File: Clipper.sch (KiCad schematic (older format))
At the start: 38 parts

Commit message: Added component numbers.
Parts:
- gave numbers to parts that had none: 35
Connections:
- net AGND: now also U17.3 (+), U17.5 (+), U18.3 (+); no longer U17.3 (+), U17.5 (+), U18.5 (+)
- net LOUT: now also U17.1; no longer U17.7
- net at R37.2, R38.2, R39.2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: now also U17.2 (_); no longer U17.6 (_)
- net at D20.1 (A), R41.2, R43.1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: now also U17.6 (_); no longer U17.2 (_)
- net at D20.2 (K), D22.1 (A): now also U17.7; no longer U17.1
- net at D21.1 (A), R42.2, R44.2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: now also U18.2 (_); no longer U18.6 (_)
- net at D21.2 (K), D23.1 (A): now also U18.1; no longer U18.7
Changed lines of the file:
@@
 LOUT
 $Comp
-L R R?
+L R R31
 U 1 1 536E7249
 P 1450 3050
-F 0 "R?" V 1530 3050 40  0000 C CNN
+F 0 "R31" V 1530 3050 40  0000 C CNN
 F 1 "12k" V 1450 3050 40  0000 C CNN
 F 2 "~" V 1380 3050 30  0000 C CNN
@@
 $EndComp
 $Comp
-L R R?
+L R R33
 U 1 1 536E7262
 P 1850 2600
-F 0 "R?" V 1930 2600 40  0000 C CNN
+F 0 "R33" V 1930 2600 40  0000 C CNN
 F 1 "30k" V 1857 2601 40  0000 C CNN
 F 2 "~" V 1780 2600 30  0000 C CNN
@@
 $EndComp
 $Comp
-L LM4562 U?
+L LM4562 U16
 U 1 1 536E7276
 P 2500 3150
-F 0 "U?" H 2750 3000 60  0000 L CNN
+F 0 "U16" H 2750 3000 60  0000 L CNN
 F 1 "LM4562" H 2750 2900 60  0000 L CNN
 F 2 "~" H 2600 3150 60  0000 C CNN
@@
 -15V
 $Comp
-L DIODE D?
+L DIODE D16
 U 1 1 536E72A5
 P 2600 2550
-F 0 "D?" H 2600 2650 40  0000 C CNN
+F 0 "D16" H 2600 2650 40  0000 C CNN
 F 1 "1N4148" H 2600 2450 40  0000 C CNN
 F 2 "~" H 2600 2550 60  0000 C CNN
@@
 $EndComp
 $Comp
-L DIODE D?
+L DIODE D18
 U 1 1 536E72BC
 P 2900 2250
-F 0 "D?" H 2900 2350 40  0000 C CNN
+F 0 "D18" H 2900 2350 40  0000 C CNN
 F 1 "1N4148" H 2900 2150 40  0000 C CNN
 F 2 "~" H 2900 2250 60  0000 C CNN
@@
 $EndComp
 $Comp
-L R R?
+L R R35
 U 1 1 536E72D9
 P 2350 2250
-F 0 "R?" V 2430 2250 40  0000 C CNN
+F 0 "R35" V 2430 2250 40  0000 C CNN
 F 1 "12k" V 2357 2251 40  0000 C CNN
 F 2 "~" V 2280 2250 30  0000 C CNN
@@
 +15V
 $Comp
-L R R?
+L R R32
 U 1 1 536E799F
 P 1450 4950
-F 0 "R?" V 1530 4950 40  0000 C CNN
+F 0 "R32" V 1530 4950 40  0000 C CNN
 F 1 "12k" V 1450 4950 40  0000 C CNN
 F 2 "~" V 1380 4950 30  0000 C CNN
@@
 $EndComp
 $Comp
-L R R?
+L R R34
 U 1 1 536E79A5
 P 1850 5400
-F 0 "R?" V 1930 5400 40  0000 C CNN
+F 0 "R34" V 1930 5400 40  0000 C CNN
 F 1 "30k" V 1857 5401 40  0000 C CNN
 F 2 "~" V 1780 5400 30  0000 C CNN
@@
 $EndComp
 $Comp
-L LM4562 U?
+L LM4562 U16
 U 2 1 536E79AB
 P 2500 5050
-F 0 "U?" H 2750 4900 60  0000 L CNN
+F 0 "U16" H 2750 4900 60  0000 L CNN
 F 1 "LM4562" H 2750 4800 60  0000 L CNN
 F 2 "~" H 2600 5050 60  0000 C CNN
@@
 -15V
 $Comp
-L DIODE D?
+L DIODE D17
 U 1 1 536E79B4
 P 2600 4450
-F 0 "D?" H 2600 4550 40  0000 C CNN
+F 0 "D17" H 2600 4550 40  0000 C CNN
 F 1 "1N4148" H 2600 4350 40  0000 C CNN
 F 2 "~" H 2600 4450 60  0000 C CNN
@@
 $EndComp
 $Comp
-L DIODE D?
+L DIODE D19
 U 1 1 536E79BA
 P 2900 4150
-F 0 "D?" H 2900 4250 40  0000 C CNN
+F 0 "D19" H 2900 4250 40  0000 C CNN
 F 1 "1N4148" H 2900 4050 40  0000 C CNN
 F 2 "~" H 2900 4150 60  0000 C CNN
@@
 $EndComp
 $Comp
-L R R?
+L R R36
 U 1 1 536E79C0
 P 2350 4150
-F 0 "R?" V 2430 4150 40  0000 C CNN
+F 0 "R36" V 2430 4150 40  0000 C CNN
 F 1 "12k" V 2357 4151 40  0000 C CNN
 F 2 "~" V 2280 4150 30  0000 C CNN
@@
 -15V
 $Comp
-L LM4562 U?
-U 2 1 536E7B83
+L LM4562 U17
+U 1 1 536E7B83
 P 4650 3800
-F 0 "U?" H 4900 3650 60  0000 L CNN
+F 0 "U17" H 4900 3650 60  0000 L CNN
 F 1 "LM4562" H 4900 3550 60  0000 L CNN
 F 2 "~" H 4750 3800 60  0000 C CNN
 F 3 "~" H 4750 3800 60  0000 C CNN
-	2    4650 3800
+	1    4650 3800
 	1    0    0    -1
 $EndComp
@@
 -15V
 $Comp
-L R R?
+L R R41
 U 1 1 536E8357
 P 6850 3050
-F 0 "R?" V 6930 3050 40  0000 C CNN
+F 0 "R41" V 6930 3050 40  0000 C CNN
 F 1 "12k" V 6850 3050 40  0000 C CNN
 F 2 "~" V 6780 3050 30  0000 C CNN
@@
 $EndComp
 $Comp
-L R R?
+L R R43
 U 1 1 536E835D
 P 7250 2600
-F 0 "R?" V 7330 2600 40  0000 C CNN
+F 0 "R43" V 7330 2600 40  0000 C CNN
 F 1 "30k" V 7257 2601 40  0000 C CNN
 F 2 "~" V 7180 2600 30  0000 C CNN
@@
 $EndComp
 $Comp
-L LM4562 U?
-U 1 1 536E8363
+L LM4562 U17
+U 2 1 536E8363
 P 7900 3150
-F 0 "U?" H 8150 3000 60  0000 L CNN
+F 0 "U17" H 8150 3000 60  0000 L CNN
 F 1 "LM4562" H 8150 2900 60  0000 L CNN
 F 2 "~" H 8000 3150 60  0000 C CNN
 F 3 "~" H 8000 3150 60  0000 C CNN
-	1    7900 3150
+	2    7900 3150
 	1    0    0    -1
 $EndComp
@@
 -15V
 $Comp
-L DIODE D?
+L DIODE D20
 U 1 1 536E836C
 P 8000 2550
-F 0 "D?" H 8000 2650 40  0000 C CNN
+F 0 "D20" H 8000 2650 40  0000 C CNN
 F 1 "1N4148" H 8000 2450 40  0000 C CNN
 F 2 "~" H 8000 2550 60  0000 C CNN
@@
 $EndComp
 $Comp
-L DIODE D?
+L DIODE D22
 U 1 1 536E8372
 P 8300 2250
-F 0 "D?" H 8300 2350 40  0000 C CNN
+F 0 "D22" H 8300 2350 40  0000 C CNN
 F 1 "1N4148" H 8300 2150 40  0000 C CNN
 F 2 "~" H 8300 2250 60  0000 C CNN
@@
 $EndComp
 $Comp
-L R R?
+L R R45
 U 1 1 536E8378
 P 7750 2250
-F 0 "R?" V 7830 2250 40  0000 C CNN
+F 0 "R45" V 7830 2250 40  0000 C CNN
 F 1 "12k" V 7757 2251 40  0000 C CNN
 F 2 "~" V 7680 2250 30  0000 C CNN
@@
 +15V
 $Comp
-L R R?
+L R R42
 U 1 1 536E8391
 P 6850 4950
-F 0 "R?" V 6930 4950 40  0000 C CNN
+F 0 "R42" V 6930 4950 40  0000 C CNN
 F 1 "12k" V 6850 4950 40  0000 C CNN
 F 2 "~" V 6780 4950 30  0000 C CNN
@@
 $EndComp
 $Comp
-L R R?
+L R R44
 U 1 1 536E8397
 P 7250 5400
-F 0 "R?" V 7330 5400 40  0000 C CNN
+F 0 "R44" V 7330 5400 40  0000 C CNN
 F 1 "30k" V 7257 5401 40  0000 C CNN
 F 2 "~" V 7180 5400 30  0000 C CNN
@@
 $EndComp
 $Comp
-L LM4562 U?
-U 2 1 536E839D
+L LM4562 U18
+U 1 1 536E839D
 P 7900 5050
-F 0 "U?" H 8150 4900 60  0000 L CNN
+F 0 "U18" H 8150 4900 60  0000 L CNN
 F 1 "LM4562" H 8150 4800 60  0000 L CNN
 F 2 "~" H 8000 5050 60  0000 C CNN
 F 3 "~" H 8000 5050 60  0000 C CNN
-	2    7900 5050
+	1    7900 5050
 	1    0    0    -1
 $EndComp
@@
 -15V
 $Comp
-L DIODE D?
+L DIODE D21
 U 1 1 536E83A6
 P 8000 4450
-F 0 "D?" H 8000 4550 40  0000 C CNN
+F 0 "D21" H 8000 4550 40  0000 C CNN
 F 1 "1N4148" H 8000 4350 40  0000 C CNN
 F 2 "~" H 8000 4450 60  0000 C CNN
@@
 $EndComp
 $Comp
-L DIODE D?
+L DIODE D23
 U 1 1 536E83AC
 P 8300 4150
-F 0 "D?" H 8300 4250 40  0000 C CNN
+F 0 "D23" H 8300 4250 40  0000 C CNN
 F 1 "1N4148" H 8300 4050 40  0000 C CNN
 F 2 "~" H 8300 4150 60  0000 C CNN
@@
 $EndComp
 $Comp
-L R R?
+L R R46
 U 1 1 536E83B2
 P 7750 4150
-F 0 "R?" V 7830 4150 40  0000 C CNN
+F 0 "R46" V 7830 4150 40  0000 C CNN
 F 1 "12k" V 7757 4151 40  0000 C CNN
 F 2 "~" V 7680 4150 30  0000 C CNN
@@
 -15V
 $Comp
-L LM4562 U?
+L LM4562 U18
 U 2 1 536E83E9
 P 10050 3800
-F 0 "U?" H 10300 3650 60  0000 L CNN
+F 0 "U18" H 10300 3650 60  0000 L CNN
 F 1 "LM4562" H 10300 3550 60  0000 L CNN
 F 2 "~" H 10150 3800 60  0000 C CNN
@@
 Set to clip at +/- 6 V
 $Comp
-L C C?
+L C C38
 U 1 1 536EC1E0
 P 5450 1700
-F 0 "C?" H 5450 1800 40  0000 L CNN
+F 0 "C38" H 5450 1800 40  0000 L CNN
 F 1 "470n" H 5456 1615 40  0000 L CNN
 F 2 "~" H 5488 1550 30  0000 C CNN
@@
 	5250 1900 5800 1900
 $Comp
-L C C?
+L C C40
 U 1 1 537C3D88
 P 5800 1700
-F 0 "C?" H 5800 1800 40  0000 L CNN
+F 0 "C40" H 5800 1800 40  0000 L CNN
 F 1 "470n" H 5806 1615 40  0000 L CNN
 F 2 "~" H 5838 1550 30  0000 C CNN
@@
 $EndComp
 $Comp
-L C C?
+L C C39
 U 1 1 537C3D8F
 P 5450 2100
-F 0 "C?" H 5450 2200 40  0000 L CNN
+F 0 "C39" H 5450 2200 40  0000 L CNN
 F 1 "470n" H 5456 2015 40  0000 L CNN
 F 2 "~" H 5488 1950 30  0000 C CNN
@@
 $EndComp
 $Comp
-L C C?
+L C C41
 U 1 1 537C3D96
 P 5800 2100
-F 0 "C?" H 5800 2200 40  0000 L CNN
+F 0 "C41" H 5800 2200 40  0000 L CNN
 F 1 "470n" H 5806 2015 40  0000 L CNN
 F 2 "~" H 5838 1950 30  0000 C CNN
@@
 $EndComp
 $Comp
-L R R?
+L R R37
 U 1 1 537C500E
 P 3600 3400
-F 0 "R?" V 3680 3400 40  0000 C CNN
+F 0 "R37" V 3680 3400 40  0000 C CNN
 F 1 "2.2k" V 3607 3401 40  0000 C CNN
 F 2 "~" V 3530 3400 30  0000 C CNN
@@
 Noise calculation:\nFull scale approx. +/- 6V.\n24 bits, so LSB corresponds to approx. 12*2^(-24) = 0.72 uV.\nQucs analysis gives a pretty flat noise spectrum at around 0.4 uV, which passes.
 $Comp
-L R R?
+L R R38
 U 1 1 537CA2E9
 P 3600 3700
-F 0 "R?" V 3680 3700 40  0000 C CNN
+F 0 "R38" V 3680 3700 40  0000 C CNN
 F 1 "2.2k" V 3607 3701 40  0000 C CNN
 F 2 "~" V 3530 3700 30  0000 C CNN
@@
 $EndComp
 $Comp
-L R R?
+L R R39
 U 1 1 537CA2EF
 P 3600 4000
-F 0 "R?" V 3680 4000 40  0000 C CNN
+F 0 "R39" V 3680 4000 40  0000 C CNN
 F 1 "2.2k" V 3607 4001 40  0000 C CNN
 F 2 "~" V 3530 4000 30  0000 C CNN
@@
 $EndComp
 $Comp
-L R R?
+L R R40
 U 1 1 537CA2F5
 P 4750 3200
-F 0 "R?" V 4830 3200 40  0000 C CNN
+F 0 "R40" V 4830 3200 40  0000 C CNN
 F 1 "2.2k" V 4757 3201 40  0000 C CNN
 F 2 "~" V 4680 3200 30  0000 C CNN
@@
 $EndComp
 $Comp
-L R R?
+L R R47
 U 1 1 537CA2FB
 P 9000 3400
-F 0 "R?" V 9080 3400 40  0000 C CNN
+F 0 "R47" V 9080 3400 40  0000 C CNN
 F 1 "2.2k" V 9007 3401 40  0000 C CNN
 F 2 "~" V 8930 3400 30  0000 C CNN
@@
 $EndComp
 $Comp
-L R R?
+L R R48
 U 1 1 537CA301
 P 9000 3700
-F 0 "R?" V 9080 3700 40  0000 C CNN
+F 0 "R48" V 9080 3700 40  0000 C CNN
 F 1 "2.2k" V 9007 3701 40  0000 C CNN
 F 2 "~" V 8930 3700 30  0000 C CNN
@@
 $EndComp
 $Comp
-L R R?
+L R R49
 U 1 1 537CA307
 P 9000 4000
-F 0 "R?" V 9080 4000 40  0000 C CNN
+F 0 "R49" V 9080 4000 40  0000 C CNN
 F 1 "2.2k" V 9007 4001 40  0000 C CNN
 F 2 "~" V 8930 4000 30  0000 C CNN
@@
 $EndComp
 $Comp
-L R R?
+L R R50
 U 1 1 537CA30D
 P 10150 3200
-F 0 "R?" V 10230 3200 40  0000 C CNN
+F 0 "R50" V 10230 3200 40  0000 C CNN
 F 1 "2.2k" V 10157 3201 40  0000 C CNN
 F 2 "~" V 10080 3200 30  0000 C CNN

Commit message: Minor schematic mods, started assigning DigiKey part numbers to components.
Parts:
- C38, C39, C40, C41: DigiKey (none) -> 445-8425-ND; Type Ceramic -> (none)
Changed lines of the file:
@@
 LIBS:my-conn
 LIBS:ADC-cache
-EELAYER 27 0
+EELAYER 24 0
 EELAYER END
 $Descr A4 11693 8268
@@
 F 2 "~" H 5488 1550 30  0000 C CNN
 F 3 "~" H 5450 1700 60  0000 C CNN
-F 4 "Ceramic" H 5450 1700 60  0001 C CNN "Type"
+F 4 "445-8425-ND" H 5450 1700 60  0001 C CNN "DigiKey"
 	1    5450 1700
 	1    0    0    -1
@@
 Wire Wire Line
 	5250 1900 5800 1900
-$Comp
-L C C40
-U 1 1 537C3D88
-P 5800 1700
-F 0 "C40" H 5800 1800 40  0000 L CNN
-F 1 "470n" H 5806 1615 40  0000 L CNN
-F 2 "~" H 5838 1550 30  0000 C CNN
-F 3 "~" H 5800 1700 60  0000 C CNN
-F 4 "Ceramic" H 5800 1700 60  0001 C CNN "Type"
-	1    5800 1700
-	1    0    0    -1
-$EndComp
-$Comp
-L C C39
-U 1 1 537C3D8F
-P 5450 2100
-F 0 "C39" H 5450 2200 40  0000 L CNN
-F 1 "470n" H 5456 2015 40  0000 L CNN
-F 2 "~" H 5488 1950 30  0000 C CNN
-F 3 "~" H 5450 2100 60  0000 C CNN
-F 4 "Ceramic" H 5450 2100 60  0001 C CNN "Type"
-	1    5450 2100
-	1    0    0    -1
-$EndComp
-$Comp
-L C C41
-U 1 1 537C3D96
-P 5800 2100
-F 0 "C41" H 5800 2200 40  0000 L CNN
-F 1 "470n" H 5806 2015 40  0000 L CNN
-F 2 "~" H 5838 1950 30  0000 C CNN
-F 3 "~" H 5800 2100 60  0000 C CNN
-F 4 "Ceramic" H 5800 2100 60  0001 C CNN "Type"
-	1    5800 2100
-	1    0    0    -1
-$EndComp
 $Comp
 L R R37
@@
 	0    -1   -1   0
 $EndComp
+$Comp
+L C C40
+U 1 1 537D7769
+P 5800 1700
+F 0 "C40" H 5800 1800 40  0000 L CNN
+F 1 "470n" H 5806 1615 40  0000 L CNN
+F 2 "~" H 5838 1550 30  0000 C CNN
+F 3 "~" H 5800 1700 60  0000 C CNN
+F 4 "445-8425-ND" H 5800 1700 60  0001 C CNN "DigiKey"
+	1    5800 1700
+	1    0    0    -1
+$EndComp
+$Comp
+L C C39
+U 1 1 537D7778
+P 5450 2100
+F 0 "C39" H 5450 2200 40  0000 L CNN
+F 1 "470n" H 5456 2015 40  0000 L CNN
+F 2 "~" H 5488 1950 30  0000 C CNN
+F 3 "~" H 5450 2100 60  0000 C CNN
+F 4 "445-8425-ND" H 5450 2100 60  0001 C CNN "DigiKey"
+	1    5450 2100
+	1    0    0    -1
+$EndComp
+$Comp
+L C C41
+U 1 1 537D7787
+P 5800 2100
+F 0 "C41" H 5800 2200 40  0000 L CNN
+F 1 "470n" H 5806 2015 40  0000 L CNN
+F 2 "~" H 5838 1950 30  0000 C CNN
+F 3 "~" H 5800 2100 60  0000 C CNN
+F 4 "445-8425-ND" H 5800 2100 60  0001 C CNN "DigiKey"
+	1    5800 2100
+	1    0    0    -1
+$EndComp
 $EndSCHEMATC

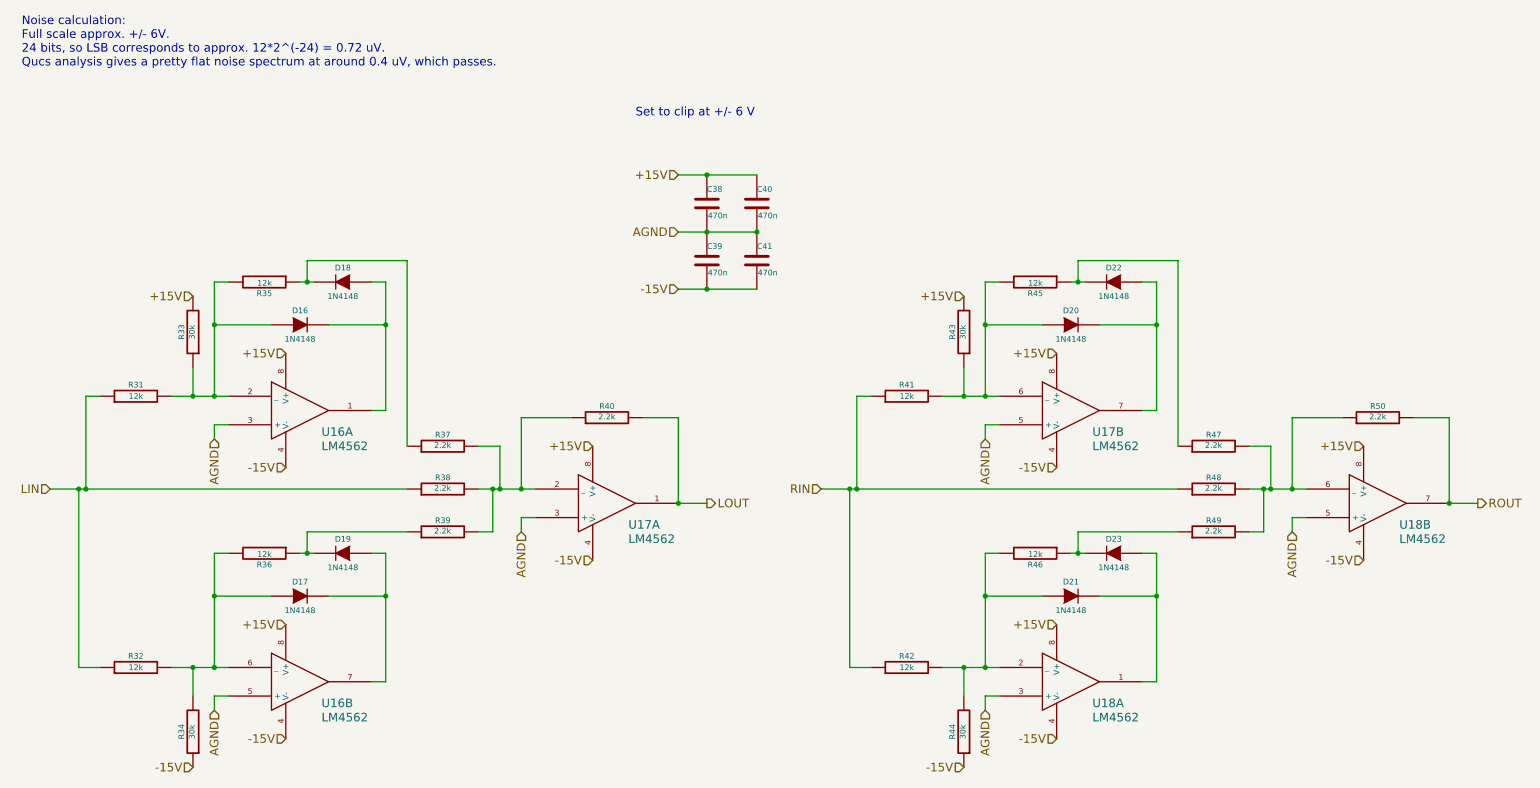
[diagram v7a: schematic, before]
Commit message: Further component specifications for the BOM.
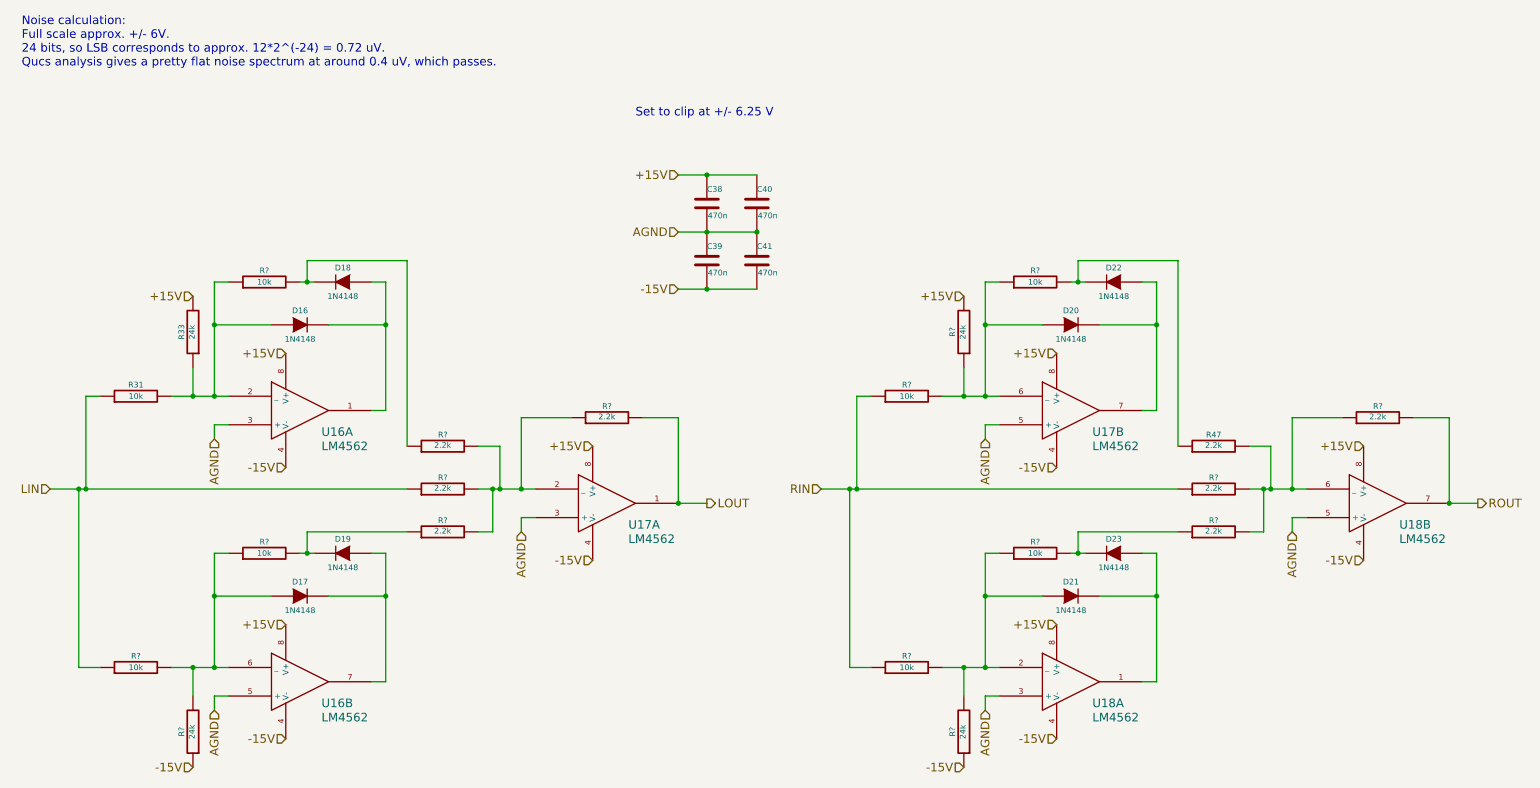
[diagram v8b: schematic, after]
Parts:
- removed R32, R35, R36, R41, R42, R45, R46: 12k, ~, symbol R
- removed R34, R43, R44: 30k, ~, symbol R
- removed R37, R38, R39, R40, R48, R49, R50: 2.2k, ~, symbol R
- added R? (x3): 24k, ~, symbol R
- added R? (x7): 10k, ~, symbol R
- added R? (x7): 2.2k, ~, symbol R
- R31: value 12k -> 10k; DigiKey (none) -> 10KADCT-ND
- R33: value 30k -> 24k; DigiKey (none) -> S24KCACT-ND
- R47: DigiKey (none) -> 2.2KADCT-ND
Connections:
- net +15V: now also R?.2
- net -15V: now also R?.1, R?.1
- net LIN: now also R?.1, R?.1
- net LOUT: now also R?.2
- net RIN: now also R?.1, R?.1, R?.1
- net ROUT: now also R?.2
- net at D16.1 (A), R31.2, R33.1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: now also R?.1
- net at D18.2 (K): now also R?.1, R?.2
- net at D17.1 (A), U16.6 (_): now also R?.1, R?.2, R?.2
- net at D19.2 (K): now also R?.1, R?.2
- net at U17.2 (_): now also R?.1, R?.2, R?.2, R?.2
- net at D20.1 (A), U17.6 (_): now also R?.1, R?.1, R?.2
- net at D22.2 (K), R47.1: now also R?.2
- net at D21.1 (A), U18.2 (_): now also R?.1, R?.2, R?.2
- net at D23.2 (K): now also R?.1, R?.2
- net at R47.2, U18.6 (_): now also R?.1, R?.2, R?.2
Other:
- note added: "Set to clip at +/- 6.25 V"
- note removed: "Set to clip at +/- 6 V"
